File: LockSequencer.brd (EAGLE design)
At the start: 100 x 80 mm, 37 parts, among them IC1 4017D, IC2 NE555, K1 G2RA, K2 G2RA

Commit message: Complete versions of the SPICE and Eagle schmatic
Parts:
- removed C10: 100n, rcl:C025-024X044
- removed C8: 10n, rcl:C025-024X044
- removed D5: 1N4004, diode:DO41-10
- removed F1, F2: FUSEKS9V, fuse:KS9V
- removed JP2, JP3, JP4: (no value), pinhead:2X02
- removed X2, X3: (no value), con-wago-500:W237-102
- added C11, C14: 100n, rcl:C050-024X044
- added C12: 10n, rcl:C1206K
- added C13: 10uF, rcl:E2-5
- added D11, D8: P6KEXXC, diode:CB417-15
- added D6, D9: UF5404, diode:CB429-15
- added D7: 1N5819-T, diode:DO41-7.6
- added F3, F4, F5, F6: (no value), fuse:TE5
- added JP5, JP6, JP7: (no value), pinhead:2X02
- added LED1, LED2, LED3, LED4: (no value), led:LED5MM
- added R10, R11, R14, R16: 15K4, rcl:R0603
- added R12, R15, R17: 2K2, rcl:0207/7
- added R13: 15K4, rcl:0207/7
- added R18, R19: 0R1, rcl:R2512
- added R20: 7K5, rcl:0207/7
- added R6, R7: 10K, rcl:R0805
- added R8: 2K2, rcl:R0402
- added R9: 196R, rcl:R0805
- added T4: (no value), transistor:SOT23-BEC
- added T5: (no value), transistor:SOT23
- added U$1, U$13: 2N7002, transistor-fet:SOT23
- added X4, X5, X6, X7, X8, X9: (no value), con-wago-500:W237-102
- C1: value 100uF -> 330uF; device rcl:085CS_1AR -> rcl:E3,5-8
- C2: value 100n -> 100uF; device rcl:C025-024X044 -> rcl:E2-5
- C3, C5: device rcl:C025-024X044 -> rcl:C1206K
- C4: device rcl:C025-024X044 -> rcl:C050-024X044
- C6: value 1u -> 1uF; device rcl:085CS_1AR -> rcl:C1206K
- C7: value 10n -> 100n; device rcl:C025-024X044 -> rcl:C1206K
- C9: value 100uF -> 100n; device rcl:085CS_1AR -> rcl:C1206K
- D1, D2: value 1N4004 -> P6KEXXC; device diode:DO41-10 -> diode:CB417-15
- D3: value Z3.6V -> Z12V; device diode:SOD323-R -> diode:SOD323-W
- K1, K2: value G2RA -> G2RATE-OJ; device relay:G2RA -> relay:G2RA-SHORTER
- R1: value 10k -> 10K; device rcl:0204V -> rcl:0207/7
- R2: value 10k -> 7K5; device rcl:0204V -> rcl:0207/7
- R3: value 100k -> (none); device rcl:0204V -> pot:CA9V
- R4: device rcl:0204V -> rcl:0207/7
- R5: value 1k -> 2K2; device rcl:0204V -> rcl:R0402
- T2, T3: device transistor:SOT23 -> transistor:SOT23-BEC
- moved C3 1091.6 mm to (-148.6, -1210.3)
- moved C7 766.4 mm to (-148.6, -1202.7)
- moved D3 753.3 mm to (-120.7, -791.2)
- moved D4 714.1 mm to (-129.5, -1181.1)
- moved K2 700.2 mm to (-119.4, -1027.4)
- moved T3 631.9 mm to (-92.7, -916.9)
- moved C4 591.7 mm to (-90.2, -753.1)
- moved C5 560.9 mm to (-97.8, -735.3)
- moved R3 557.7 mm to (-113.0, -744.2)
- moved T2 542.5 mm to (-97.8, -693.4)
- moved R5 541.1 mm to (-90.2, -635.0)
- moved D2 534.7 mm to (-114.3, -901.7)
- moved C6 529.3 mm to (-97.8, -743.0)
- moved C2 494.1 mm to (-87.6, -602.0)
- moved D1 468.3 mm to (-114.3, -852.2)
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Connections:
- removed net +12V: C10.1, C4.1, C7.1, C8.1, C9.+, D1.A, D1.C, D2.C, D4.C, D5.C, IC2.4, IC2.8, K1.1, K1.2, K2.1, R1.2, R4.2, R5.2, T1.3, X1.1, X2.2, X3.2
- removed net N$19: C8.2, D5.A, F1.1, X3.1
- new net N$23: R5.1, U$13.1
- new net N$24: IC2.7, R3.A, R3.S, R4.1
- new net N$25: C7.1, D3.C, R9.1, T2.B
- new net N$26: R11.2, T3.B
- new net N$27: D1.A, K1.2, LED1.K, T4.C
- new net N$28: R8.2, U$1.1
- new net N$29: LED1.A, R12.1
- new net N$30: F4.2, X5.1
- new net N$31: F3.2, X6.1
- new net N$32: JP5.1, JP5.2, JP6.1, JP6.2, JP7.1, JP7.2, R10.1
- new net N$33: JP5.3, JP5.4, JP6.3, JP6.4, JP7.3, JP7.4, R11.1
- new net N$34: LED3.A, R15.1
- new net N$35: LED3.K, T1.3
- new net N$36: R16.1, T5.1
- new net N$37: D6.A, R18.2
- new net N$38: LED4.K, T5.3
- new net N$39: D9.A, R19.2
- new net N$40: R18.1, R19.1, X7.2
- new net N$43: D11.C, K2.P, X8.2, X9.2
- new net N$44: F6.2, X8.1
- new net N$45: F5.2, X9.1
- new net RESET_N: IC2.4, R7.1, U$1.3
- new net VEXTERNAL: D4.A, D7.A, K1.S, K2.S, X1.1, X4.1, X4.2
- new net VSUPPLY: C1.+, C11.1, D1.C, D2.C, D7.C, K1.1, K2.1, R12.2, R13.2, R9.2, T2.C
- net GND: now also C11.2, C12.2, C13.-, C14.2, C2.-, C6.2, C7.2, C9.2, D11.A, D8.A, F3.1, F4.1, F5.1, F6.1, R20.1, T3.E, T4.E, T5.2, U$1.2, U$13.2, X7.1; no longer C10.2, C2.2, C3.2, C6.-, C9.-, K1.P, K2.P, T2.2, T3.2
- net N$14: now also C6.1, IC2.2, IC2.6, R3.E; no longer C6.+, IC2.7, R3.1, R4.1
- net N$15: now also R10.2, T4.B; no longer IC2.2, IC2.6, R3.2
- net N$16: now also R14.1; no longer JP2.1, JP2.2, JP3.1, JP3.2, JP4.1, JP4.2
- net N$17: now also LED4.A, R17.1; no longer JP2.3, JP2.4, JP3.3, JP3.4, JP4.3, JP4.4, T3.1
- net N$18: now also LED2.K, T3.C; no longer T3.3
- net N$2: now also C2.+, C9.1; no longer C1.+, C2.1, D3.C
- net N$20: now also D4.C, R20.2; no longer C7.2, D4.A, F2.1, X2.1
- net N$21: now also D6.C, D8.C, D9.C, K1.P, X5.2, X6.2; no longer F2.2, K1.S
- net N$22: now also LED2.A, R13.1; no longer F1.2, K2.S
- net N$3: now also C12.1, R5.2; no longer T2.1
- net N$4: now also R14.2
- net N$5: now also R16.2
- net RESET: now also R6.1, R8.1, U$13.3; no longer C3.1, R5.1, T2.3
- net VDD: now also C13.+, C14.1, C3.1, C4.1, IC2.8, R1.2, R15.2, R17.2, R4.2, R6.2, R7.2, T2.E
- net VSS: now also C3.2

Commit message: Initial Component placement, removed current sinking to detect polarity
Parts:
- removed D4: 1N4004, diode:DO41-10
- removed R20: 7K5, rcl:0207/7
- removed X4: (no value), con-wago-500:W237-102
- added F1: (no value), fuse:TE5
- added X2, X3: (no value), con-wago-500:W237-102
- R12, R13, R15, R17: device rcl:0207/7 -> rcl:0207/2V
- R3: value (none) -> 220K
- moved C7 1262.5 mm to (21.6, 48.3), flipped to the bottom
- moved C3 1261.1 mm to (109.2, 24.1), turned to 270 degrees
- moved D9 1224.0 mm to (59.7, 68.6), turned to 270 degrees
- moved X7 1222.9 mm to (92.7, 40.0), turned to 90 degrees
- moved R19 1207.4 mm to (78.7, 39.4), flipped to the bottom
- moved F4 1206.0 mm to (87.6, 63.5)
- moved F3 1189.0 mm to (76.2, 63.5)
- moved D8 1177.3 mm to (96.5, 68.6), turned to 270 degrees
- moved X6 1159.6 mm to (87.6, 72.4), turned to 180 degrees
- moved X5 1121.8 mm to (92.7, 52.1), turned to 90 degrees
- moved K2 1074.4 mm to (74.9, 29.2)
- moved R15 1044.3 mm to (113.0, 10.2), turned to 90 degrees
- moved JP7 1041.2 mm to (139.7, 35.6), turned to 180 degrees
- moved JP6 1028.9 mm to (139.7, 40.6), turned to 180 degrees
- moved R14 1028.5 mm to (115.6, 15.2), turned to 90 degrees
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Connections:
- removed net GND: C1.-, C11.2, C12.2, C13.-, C14.2, C2.-, C4.2, C5.2, C6.2, C7.2, C9.2, D11.A, D3.A, D8.A, F3.1, F4.1, F5.1, F6.1, IC2.1, R2.1, R20.1, T1.2, T3.E, T4.E, T5.2, U$1.2, U$13.2, U$4.3, X1.2, X7.1
- removed net N$20: D4.C, R20.2
- new net N$19: D7.A, F1.1
- net N$43: now also X8.1; no longer X8.2
- net N$44: now also X8.2; no longer X8.1
- net VEXTERNAL: now also F1.2, X2.1, X2.2, X3.1; no longer D4.A, D7.A, X1.1, X4.1, X4.2
- net VSS: now also C1.-, C11.2, C12.2, C13.-, C14.2, C2.-, C4.2, C5.2, C6.2, C7.2, C9.2, D11.A, D3.A, D8.A, F3.1, F4.1, F5.1, F6.1, IC2.1, R2.1, T1.2, T3.E, T4.E, T5.2, U$1.2, U$13.2, U$4.3, X1.1, X1.2, X3.2, X7.1

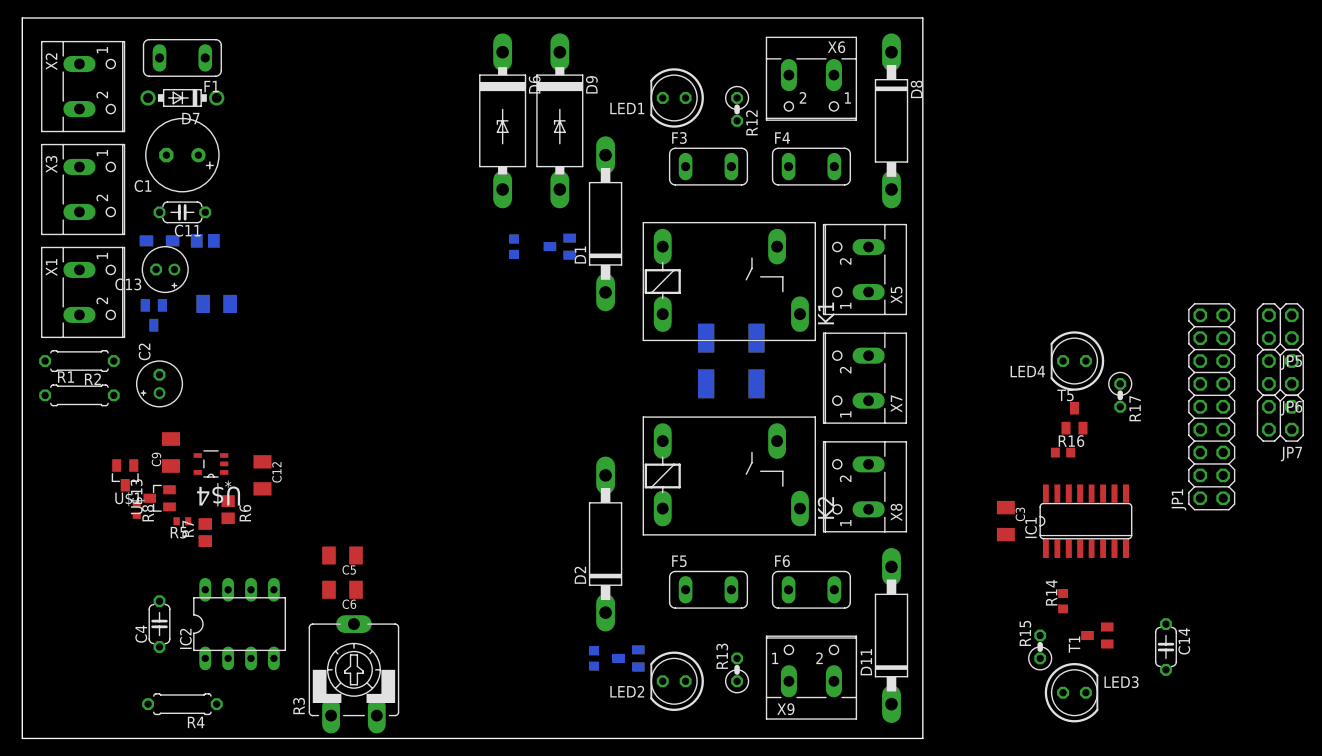
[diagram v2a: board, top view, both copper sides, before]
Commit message: Initial component placement prior to first auto routing attempt
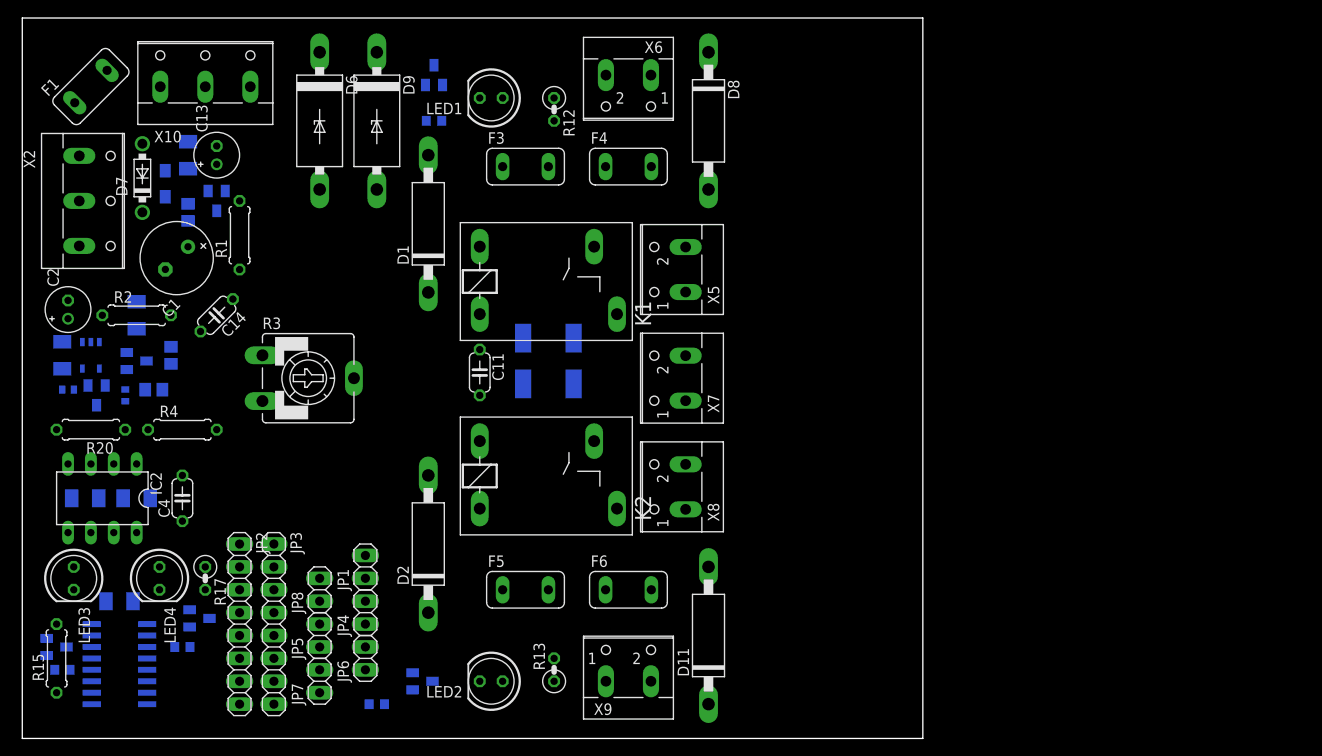
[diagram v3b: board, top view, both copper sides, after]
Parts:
- removed X1, X3: (no value), con-wago-500:W237-102
- added JP2, JP3: (no value), pinhead:1X08
- added JP4, JP8: (no value), pinhead:1X02
- added R20: 100k, rcl:0207/7
- added X10: (no value), con-wago-500:W237-103
- JP1: device pinhead:2X09 -> pinhead:1X02
- JP5, JP6, JP7: device pinhead:2X02 -> pinhead:1X02
- R15: device rcl:0207/2V -> rcl:0207/7
- X2: device con-wago-500:W237-102 -> con-wago-500:W237-103
- moved T1 115.6 mm to (3.81, 10.2), flipped to the bottom
- moved JP5 112.1 mm to (33.0, 11.4), turned to 90 degrees
- moved LED3 111.8 mm to (5.71, 17.8), turned to 270 degrees
- moved C14 111.7 mm to (21.6, 47.0), turned to 225 degrees
- moved R14 111.4 mm to (4.45, 7.62), flipped to the bottom, turned to 180 degrees
- moved JP7 110.6 mm to (33.0, 6.35), turned to 90 degrees
- moved R15 109.2 mm to (3.81, 8.89)
- moved IC1 108.5 mm to (10.8, 8.26), flipped to the bottom, turned to 270 degrees
- moved JP6 106.4 mm to (38.1, 8.89), turned to 90 degrees
- moved LED4 104.4 mm to (15.2, 17.8), turned to 270 degrees
- moved R17 103.6 mm to (20.3, 17.8)
- moved R16 100.1 mm to (17.8, 10.2), flipped to the bottom
- moved T5 99.7 mm to (19.7, 13.3), flipped to the bottom, turned to 90 degrees
- moved C3 98.8 mm to (10.8, 15.2), flipped to the bottom, turned to 180 degrees
- moved JP1 95.6 mm to (38.1, 19.1)
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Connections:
- removed net N$34: LED3.A, R15.1
- removed net N$35: LED3.K, T1.3
- removed net N$38: LED4.K, T5.3
- new net LATCH: JP1.1, JP1.2, JP4.1, JP4.2, JP6.1, JP6.2, R10.1
- new net N$20: IC1.3, R16.2
- new net OPEN: JP5.1, JP5.2, JP7.1, JP7.2, JP8.1, JP8.2, R11.1
- net N$10: now also IC1.5, JP2.6, JP3.6; no longer IC1.1, JP1.11, JP1.12
- net N$11: now also IC1.6, JP2.7, JP3.7; no longer IC1.5, JP1.13, JP1.14
- net N$12: now also IC1.9, JP2.8, JP3.8; no longer IC1.6, JP1.15, JP1.16
- net N$13: now also LED4.K, R17.1; no longer IC1.9, JP1.17, JP1.18
- net N$14: now also R20.1, R3.A; no longer R3.E
- net N$17: now also R17.2, T5.3; no longer LED4.A, R17.1
- net N$24: now also R20.2, R3.E; no longer R3.A
- net N$32: now also LED3.K, R15.2; no longer JP5.1, JP5.2, JP6.1, JP6.2, JP7.1, JP7.2, R10.1
- net N$33: now also R15.1, T1.3; no longer JP5.3, JP5.4, JP6.3, JP6.4, JP7.3, JP7.4, R11.1
- net N$5: now also IC1.2, JP2.1, JP3.1; no longer IC1.3, JP1.1, JP1.2, R16.2
- net N$6: now also IC1.4, JP2.2, JP3.2; no longer IC1.2, JP1.3, JP1.4
- net N$7: now also IC1.7, JP2.3, JP3.3; no longer IC1.4, JP1.5, JP1.6
- net N$8: now also IC1.10, JP2.4, JP3.4; no longer IC1.7, JP1.7, JP1.8
- net N$9: now also IC1.1, JP2.5, JP3.5; no longer IC1.10, JP1.10, JP1.9
- net VDD: now also LED3.A, LED4.A; no longer R15.2, R17.2
- net VEXTERNAL: now also X10.1, X10.2, X10.3; no longer X2.1, X2.2, X3.1
- net VSS: now also X2.1, X2.2, X2.3; no longer X1.1, X1.2, X3.2

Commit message: Tweaked positions
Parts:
- R17: device rcl:0207/2V -> rcl:0207/7
- moved T3 24.4 mm to (55.9, 27.9), turned to 270 degrees
- moved T4 24.1 mm to (45.7, 49.5), turned to 90 degrees
- moved R20 21.9 mm to (29.2, 30.5), turned to 270 degrees
- moved R10 20.9 mm to (40.6, 48.3), turned to 90 degrees
- moved R11 18.3 mm to (49.5, 19.1)
- moved R4 18.2 mm to (35.6, 30.5), turned to 270 degrees
- moved D8 16.8 mm to (61.0, 61.6), turned to 180 degrees
- moved D11 15.9 mm to (61.0, 15.9), turned to 180 degrees
- moved LED4 15.5 mm to (6.35, 30.5)
- moved R13 13.6 mm to (45.7, 5.08)
- moved R12 12.5 mm to (47.0, 73.0)
- moved F6 9.92 mm to (73.7, 8.89), turned to 90 degrees
- moved F5 9.25 mm to (53.3, 7.62), turned to 270 degrees
- moved LED2 8.54 mm to (46.4, 12.7), turned to 90 degrees
- moved F4 8.13 mm to (73.7, 68.6), turned to 270 degrees
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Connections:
- net N$21: now also X5.1; no longer X5.2
- net N$30: now also X5.2; no longer X5.1
- net N$43: now also X8.2; no longer X8.1
- net N$44: now also X8.1; no longer X8.2
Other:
- board size 100 x 80 mm -> 80.3 x 77.5 mm

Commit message: 555 and 4017 nearly sorted out
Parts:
- R12: device rcl:0207/2V -> rcl:0207/7
- R17: device rcl:0207/7 -> rcl:0309/12
- R6: device rcl:R0805 -> rcl:0207/7
- moved D6 67.5 mm to (96.5, 43.2)
- moved JP1 63.5 mm to (97.8, 19.1)
- moved JP4 63.5 mm to (97.8, 14.0)
- moved JP6 63.5 mm to (97.8, 8.89)
- moved D9 54.0 mm to (87.6, 41.9)
- moved JP5 45.7 mm to (85.1, 12.7)
- moved JP7 45.7 mm to (85.1, 7.62)
- moved JP8 45.7 mm to (85.1, 17.8)
- moved C1 14.6 mm to (29.2, 60.3), turned to 180 degrees
- moved R12 12.5 mm to (36.2, 66.7), turned to 225 degrees
- moved C13 8.84 mm to (18.4, 55.2), turned to 0 degrees
- moved C9 8.52 mm to (5.08, 49.5), turned to 180 degrees
- moved R1 8.52 mm to (16.5, 50.8), turned to 0 degrees
- moved D3 8.47 mm to (24.1, 62.2), turned to 180 degrees
- moved R20 7.41 mm to (25.4, 36.8), turned to 0 degrees
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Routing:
- net VDD: track 0.00 -> 62.3 mm, vias 0 -> 2
- net N$24: track 0.00 -> 46.0 mm, vias 0 -> 2
- net N$21: track 0.00 -> 37.4 mm
- net N$43: track 0.00 -> 36.6 mm
- net N$18: track 0.00 -> 34.4 mm
- net N$38: track 0.00 -> 34.0 mm, vias 0 -> 2
- net RESET: track 0.00 -> 33.1 mm
- net VSUPPLY: track 0.00 -> 32.2 mm, vias 0 -> 1
- net N$9: track 0.00 -> 26.9 mm, vias 0 -> 2
- net CLOCK: track 0.00 -> 26.7 mm
- net N$7: track 0.00 -> 26.2 mm, vias 0 -> 2
- net N$12: track 0.00 -> 25.9 mm
- net N$14: track 0.00 -> 23.8 mm
- net N$35: track 0.00 -> 21.8 mm
- net N$34: track 0.00 -> 21.8 mm
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- added copper zone on layer 1, net VDD
- added copper zone on layer 1, net VEXTERNAL
- added copper zone on layer 1, net VSS
- added copper zone on layer 16, net VSS
- added copper zone on layer 1, net VSUPPLY

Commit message: Routing completed
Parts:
- R13: device rcl:0207/2V -> rcl:0207/7
- moved JP1 60.4 mm to (37.5, 21.0)
- moved JP4 60.4 mm to (37.5, 15.9)
- moved JP6 60.4 mm to (37.5, 10.8)
- moved JP5 43.2 mm to (41.9, 11.4)
- moved JP7 43.2 mm to (41.9, 6.35)
- moved JP8 43.2 mm to (41.9, 16.5)
- moved D6 42.7 mm to (59.7, 64.8), turned to 90 degrees
- moved F4 36.2 mm to (73.7, 32.4), turned to 0 degrees
- moved R19 32.7 mm to (70.5, 73.0)
- moved D9 31.9 mm to (65.4, 64.8), turned to 90 degrees
- moved R18 29.1 mm to (65.4, 67.3)
- moved X7 27.3 mm to (73.0, 66.0)
- moved R10 24.0 mm to (45.7, 24.8), turned to 180 degrees
- moved F3 23.3 mm to (73.7, 58.4), turned to 0 degrees
- moved LED1 22.1 mm to (39.4, 44.5), turned to 0 degrees
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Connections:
- removed net N$22 (its old number): LED2.A, R13.1
- removed net N$29: LED1.A, R12.1
- removed net N$31: F3.2, X6.1
- new net N$10: LED1.K, R12.2
- new net N$11: F3.2, X6.2
- new net N$8: LED2.K, R13.2
- net N$18: now also K2.1, R13.1; no longer K2.2, LED2.K
- net N$21: now also X5.2, X6.1; no longer X5.1, X6.2
- net N$27: now also R12.1; no longer LED1.K
- net N$30: now also X5.1; no longer X5.2
- net N$43: now also K2.S, X8.1; no longer K2.P, X8.2
- net N$44: now also X8.2; no longer X8.1
- net VEXTERNAL: now also K2.P; no longer K2.S
- net VSUPPLY: now also K2.2, LED1.A, LED2.A; no longer K2.1, R12.2, R13.2
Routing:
- net VEXTERNAL: track 21.1 -> 89.9 mm
- net VSUPPLY: track 32.2 -> 89.6 mm
- net N$21: track 37.4 -> 70.7 mm
- net N$39: track 20.8 -> 0.63 mm
- net N$27: track 12.3 -> 31.4 mm
- net N$18: track 34.4 -> 16.3 mm
- net N$31: track 14.8 -> 0.00 mm
- net N$26: track 15.8 -> 3.10 mm
- net N$15: track 4.30 -> 15.5 mm
- net N$22 (its old number): track 9.83 -> 0.00 mm
- net LATCH: track 12.7 -> 21.2 mm
- net N$11: track 0.00 -> 6.30 mm
- net N$37: track 0.00 -> 5.87 mm
- net N$8: track 0.00 -> 4.71 mm
- net N$10: track 0.00 -> 4.71 mm
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- removed copper zone on layer 1, net VEXTERNAL
